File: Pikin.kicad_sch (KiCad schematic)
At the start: 22 parts, among them SW1 SW_Push, SW2 SW_Push, SW3 SW_Push, SW4 SW_Push, SW5 SW_Push, SW6 SW_Push, U1 brook_ufb

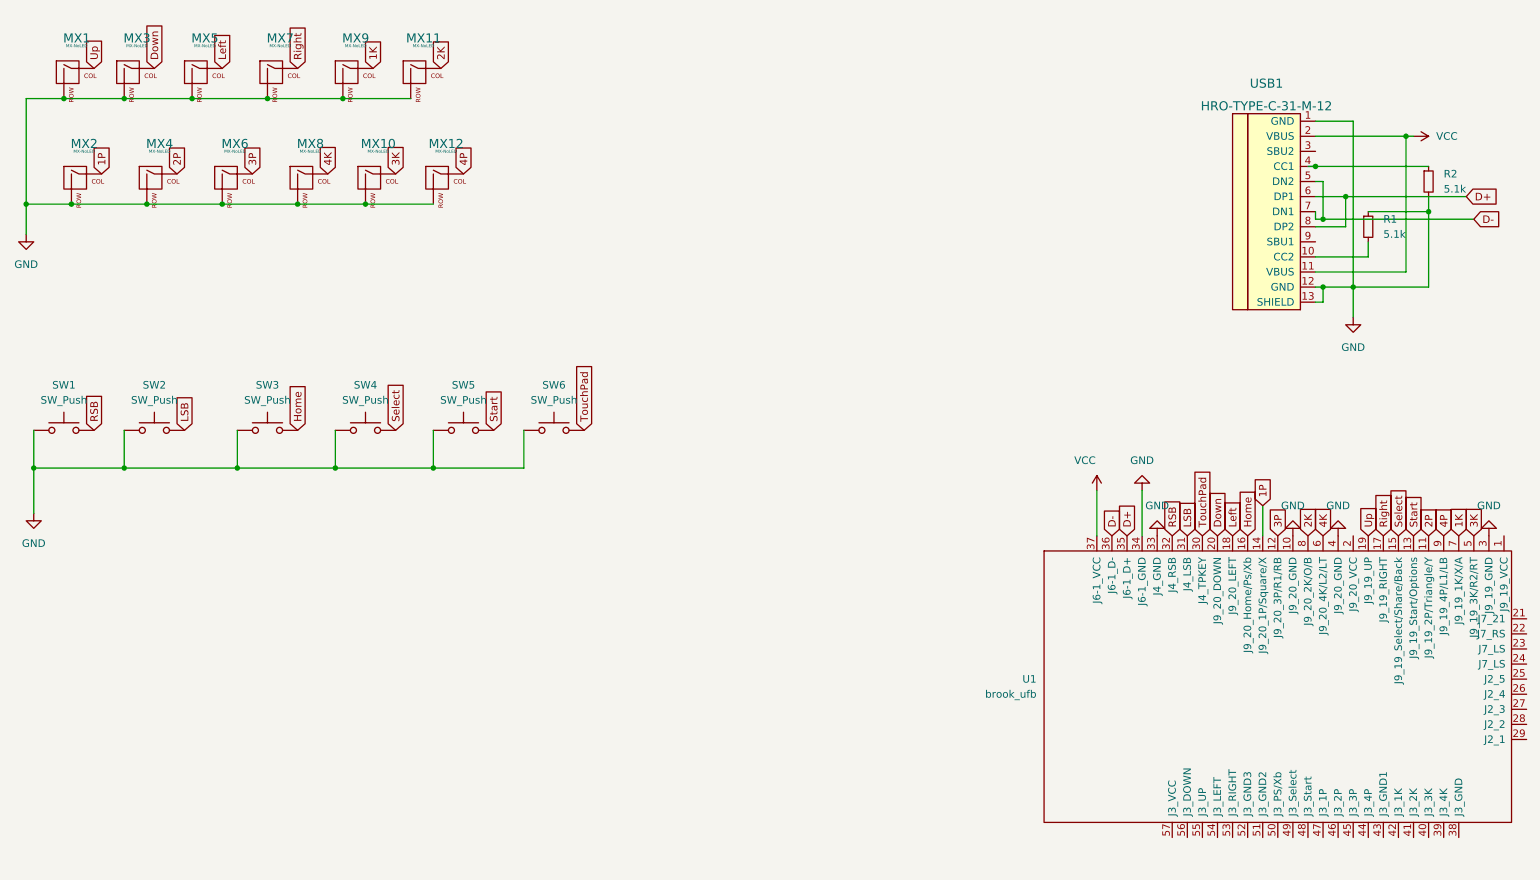
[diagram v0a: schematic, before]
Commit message: Added image files for 3D board view and layout
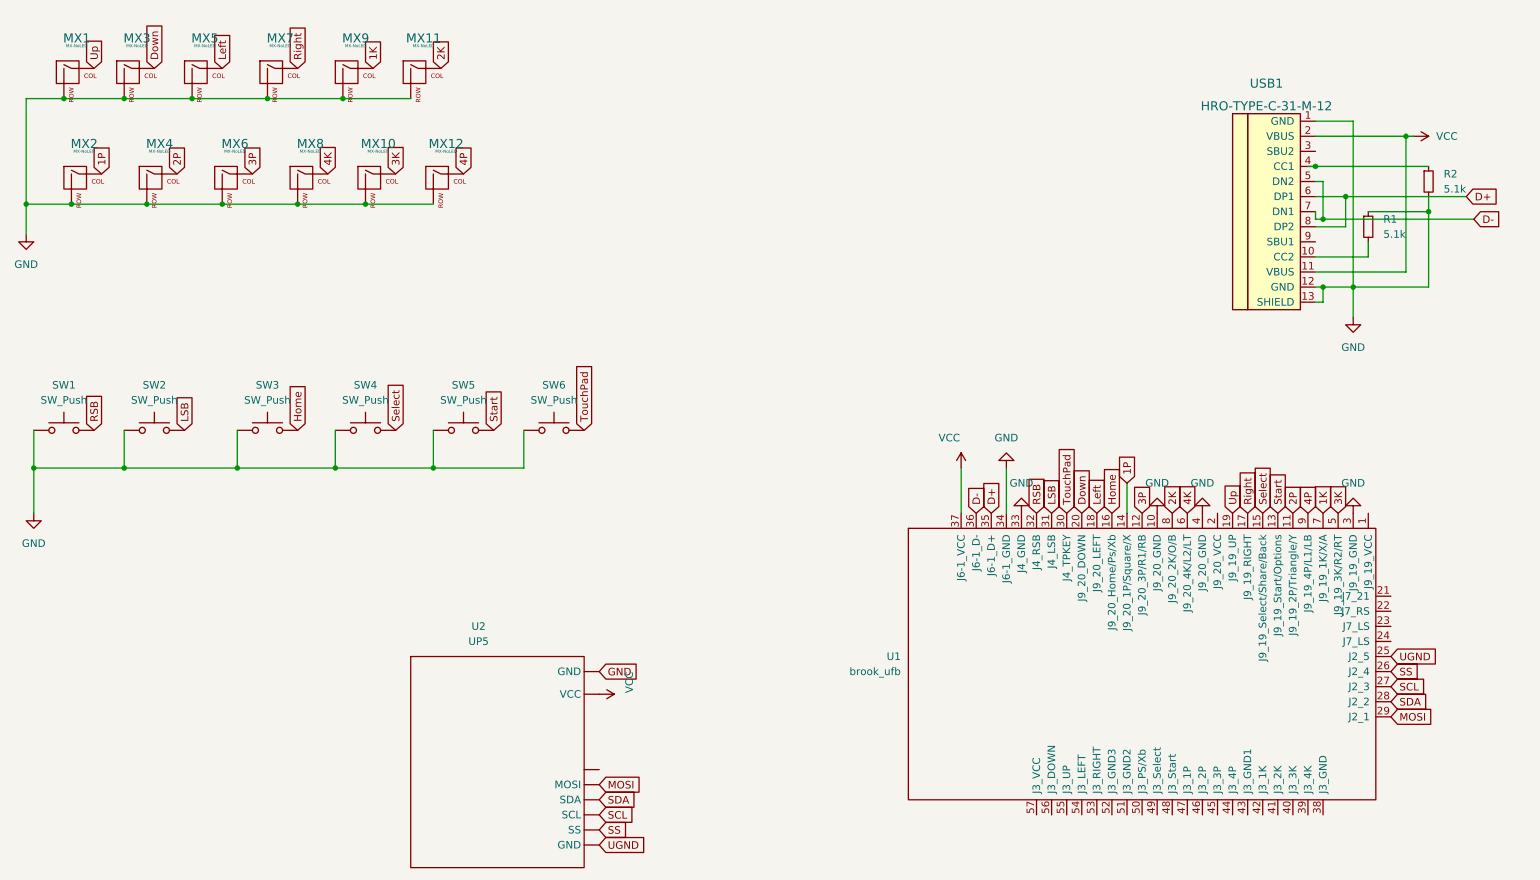
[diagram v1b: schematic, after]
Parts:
- added U2: UP5, Brook_UFB:UP5, symbol Brook:UP5
- USB1: JLPCB Part (none) -> C165948
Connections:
- net GND: now also U2. (VCC)
- net VCC: now also U2. (VCC)
- net UGND: now reaches U1.25 (J2_5)
- net UGND: now also U2. (VCC)
- net SS: now reaches U1.26 (J2_4)
- net SS: now also U2. (VCC)
- net SCL: now reaches U1.27 (J2_3)
- net SCL: now also U2. (VCC)
- net SDA: now reaches U1.28 (J2_2)
- net SDA: now also U2. (VCC)
- net MOSI: now reaches U1.29 (J2_1)
- net MOSI: now also U2. (VCC)
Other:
- moved on the sheet: U1
